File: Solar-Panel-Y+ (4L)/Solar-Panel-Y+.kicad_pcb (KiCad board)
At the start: 4 copper layers, 50 x 50 mm, 81 parts, among them J1 FTS-105-01-L-DV-A, Q1 BSS138DWQ-7, Q2 MBT2222ADW1T1, Q3 BSS138DWQ-7, Q4 MBT2222ADW1T1, U1 Value, U2 TSL2561

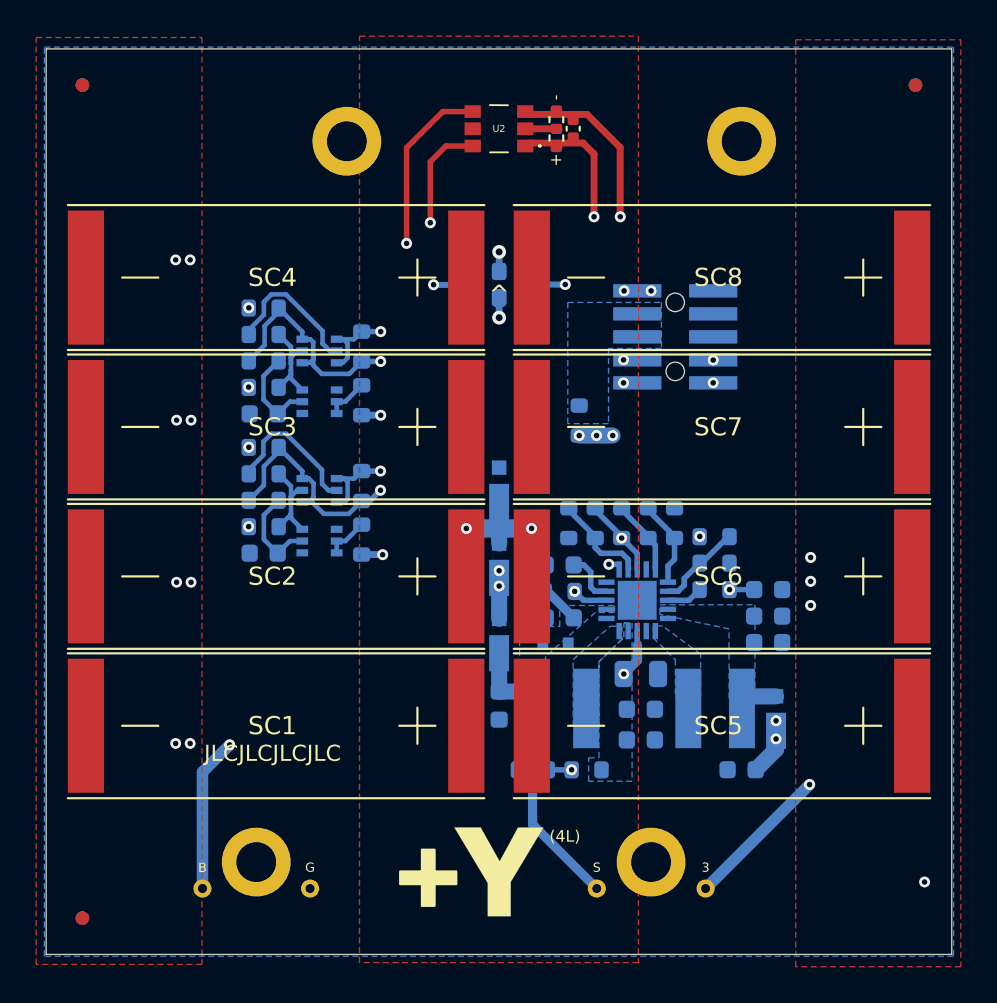
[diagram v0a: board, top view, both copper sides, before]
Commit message: Changed TSL2591 to BH1750
All boards (4L) except -Y
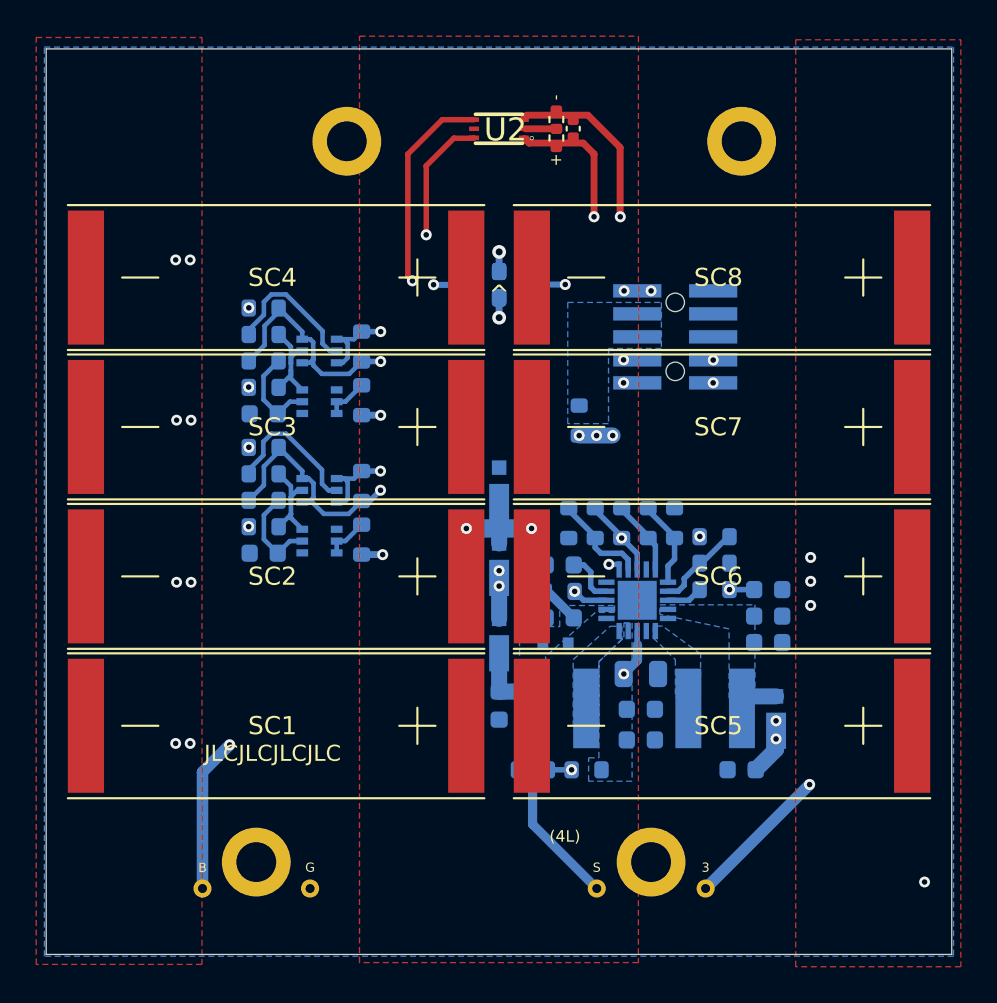
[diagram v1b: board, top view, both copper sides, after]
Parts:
- removed REF** (x6): Fiducial_0.75mm_Mask1.5mm, Fiducial:Fiducial_0.75mm_Mask1.5mm
- removed Ref**: Val**, custom-footprints:ypanel
- removed Ref**: Val**, custom-footprints:pycubed_mini_half
- U2: value TSL2561 -> BH1750FVI-TR; footprint solarpanels:TSL2561 -> solarpanels:WSOF6
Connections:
- U2 pad 4: SCL_LS -> SDA_LS
- U2 pad 6: SDA_LS -> SCL_LS
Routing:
- net SDA_LS: track 35.0 -> 36.8 mm
- net SCL_LS: track 29.7 -> 27.9 mm

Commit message: Updated light sensor to OPT 3001, Updated solar diodes.
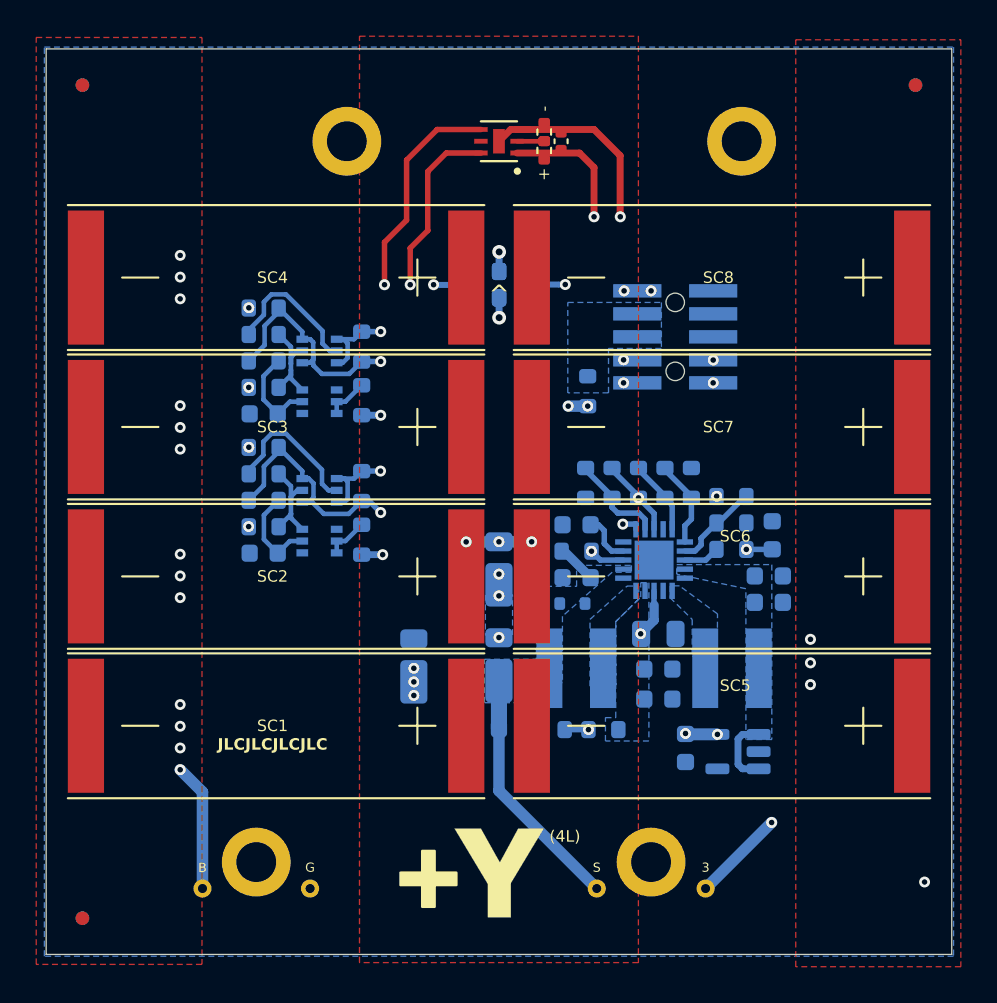
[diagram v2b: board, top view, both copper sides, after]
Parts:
- removed D5: MSS1P4-M3_89A, solarpanels:MICROSMP
- added ?: , , B.Cu at (81.6, 37.2)
- added REF**: Fiducial_0.75mm_Mask1.5mm, Fiducial:Fiducial_0.75mm_Mask1.5mm, F.Cu at (81.6, 83.2)
- added REF**: Fiducial_0.75mm_Mask1.5mm, Fiducial:Fiducial_0.75mm_Mask1.5mm, F.Cu at (81.6, 37.2)
- added REF**: Fiducial_0.75mm_Mask1.5mm, Fiducial:Fiducial_0.75mm_Mask1.5mm, F.Cu at (127.6, 37.2)
- added REF**: Fiducial_0.75mm_Mask1.5mm, Fiducial:Fiducial_0.75mm_Mask1.5mm, B.Cu at (81.6, 83.2)
- added REF**: Fiducial_0.75mm_Mask1.5mm, Fiducial:Fiducial_0.75mm_Mask1.5mm, B.Cu at (127.6, 37.2)
- added Ref**: Val**, custom-footprints:ypanel, F.Cu at (121.7, 81.6)
- added Ref**: Val**, custom-footprints:pycubed_mini_half, B.Cu at (104.7, 39.2)
- added U3: MAX40200AUK, Package_TO_SOT_SMD:SOT-23-5, B.Cu at (117.8, 74.0)
- D2, D3, D4: value MSS1P4-M3_89A -> DFLS130L-7; footprint solarpanels:MICROSMP -> Diode_SMD:D_PowerDI-123
- J1: value FTS-105-01-L-DV-A -> FTS-105-01-X-DV-A
- Q1, Q3: value BSS138DWQ-7 -> NX3008NBKS
- R1, R12, R13, R16, R17, R18, R2, R3, R4: value 0 -> 0R
- R14, R15: value DNI -> DNI (0R)
- R19: renamed from R21; value 680 -> DNI (0R)
- R20: renamed from R22; value 100K -> DNI (0R)
- R21: renamed from R19; value DNI -> 680R
- R22: renamed from R20; value DNI -> 100K
- R26: value 680 -> 680R
- U2: value BH1750FVI-TR -> OPT3001; footprint solarpanels:WSOF6 -> solarpanels:OPT3001
- moved D2 15.6 mm to (104.6, 69.2)
- moved D3 10.8 mm to (99.9, 69.3)
- moved R19 5.45 mm to (97.0, 51.6), turned to 90 degrees
- moved R21 5.45 mm to (91.6, 51.0), turned to 0 degrees
- moved R20 4.74 mm to (97.0, 59.3)
- moved R22 4.73 mm to (97.0, 54.6)
- moved C11 3.32 mm to (114.9, 73.8), turned to -90 degrees
- moved C6 3.01 mm to (119.7, 62.1), turned to 90 degrees
- moved C9 2.45 mm to (113.4, 71.1)
- moved C7 2.42 mm to (113.4, 69.4)
- moved C5 2.42 mm to (113.4, 67.5)
- moved R4 2.41 mm to (117.4, 62.8)
- moved C3 2.41 mm to (108.9, 64.4)
- moved C4 2.41 mm to (108.9, 61.5)
- moved D1 2.41 mm to (108.7, 65.8)
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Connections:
- C10 pad 1: Net-(C10-Pad1) -> Net-(U1-VOUT)
- C8 pad 1: Net-(C10-Pad1) -> Net-(U1-VOUT)
- D2 pad 1: +3V3 -> VSOLAR
- D2 pad 2: Net-(C10-Pad1) -> /VSOLAR_FULL
- L2 pad 2: Net-(C10-Pad1) -> Net-(U1-VOUT)
- Q1 pad 2: Net-(Q1-Pad2) -> Net-(Q1A-G2)
- Q1 pad 3: Net-(Q1-Pad2) -> Net-(Q1A-G2)
- Q1 pad 6: Net-(Q1-Pad6) -> Net-(Q1A-D1)
- Q2 pad 2: Net-(Q2-Pad2) -> Net-(Q2A-B1)
- Q2 pad 5: Net-(Q1-Pad6) -> Net-(Q1A-D1)
- R19 pad 1: Net-(Q2-Pad2) -> SCL_LS
- R19 pad 2: Net-(Q1-Pad6) -> SCL
- R20 pad 1: +3V3 -> SDA_LS
- R20 pad 2: Net-(Q1-Pad2) -> SDA
- R21 pad 1: SCL_LS -> Net-(Q2A-B1)
- R21 pad 2: SCL -> Net-(Q1A-D1)
- R22 pad 1: SDA_LS -> +3V3
- R22 pad 2: SDA -> Net-(Q1A-G2)
- R23 pad 2: Net-(Q1-Pad6) -> Net-(Q1A-D1)
- U1 pad 14: Net-(C10-Pad1) -> Net-(U1-VOUT)
- U2 pad 4: SDA_LS -> SCL_LS
- U2 pad 6: SCL_LS -> SDA_LS
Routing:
- net Net-(Q2A-B1): track 0.00 -> 7.79 mm
- net Net-(Q2-Pad2): track 7.79 -> 0.00 mm
- net Net-(Q1A-D1): track 0.00 -> 5.98 mm
- net Net-(Q1-Pad6): track 5.98 -> 0.00 mm
- net Net-(U1-VOUT): track 0.00 -> 3.88 mm
- net Net-(Q1A-G2): track 0.00 -> 2.40 mm
- net Net-(Q1-Pad2): track 2.40 -> 0.00 mm
- net VBAT: track 13.1 -> 10.8 mm, vias 5 -> 4
- net Net-(D3-K): track 5.89 -> 3.62 mm, vias 2 -> 6
- net Net-(C10-Pad1): track 2.05 -> 0.00 mm
- net SCL_LS: track 27.9 -> 29.9 mm
- net +3V3: track 20.2 -> 18.3 mm
- net VSOLAR: track 17.4 -> 15.8 mm
- net GND: track 10.0 -> 11.5 mm, vias 9 -> 13
- net VOUT_EN: track 9.16 -> 9.81 mm
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- added copper zone on B.Cu, net /VSOLAR_FULL
- added copper zone on B.Cu, net Net-(U1-VOUT)
- removed copper zone on B.Cu, net Net-(C10-Pad1)
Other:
- board text added: "Rev B3/01"
- board text removed: "Rev B2/01"

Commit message: Updated Mounting Holes
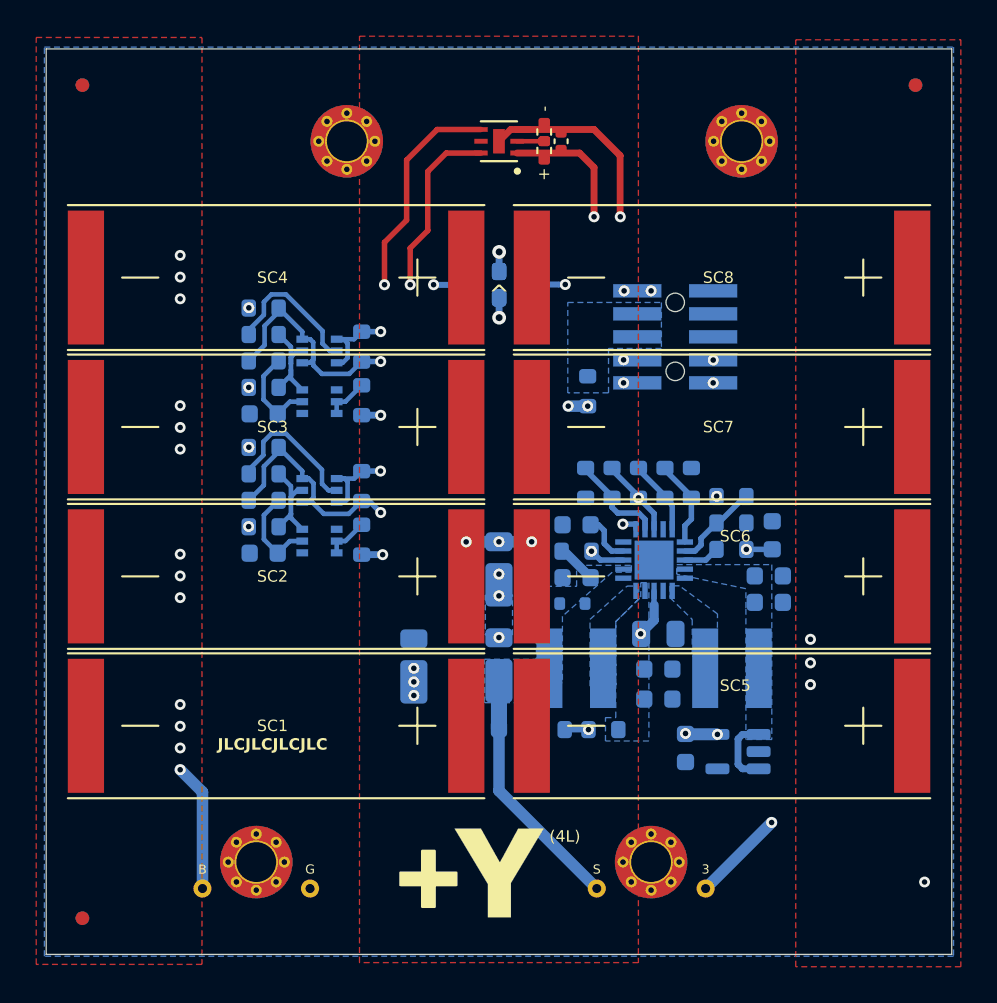
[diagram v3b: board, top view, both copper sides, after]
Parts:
- H1, H2, H3, H4: footprint MountingHole:MountingHole_2.2mm_M2_DIN965_Pad -> solarpanels:MountingHole_2.2mm_M2_DIN965_Pad_TopBottom

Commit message: B3/02 Updates
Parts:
- removed ?: , 
- added REF**: Fiducial_1mm_Mask2mm, Fiducial:Fiducial_1mm_Mask2mm, B.Cu at (81.6, 37.2)
- C1: value 1uF -> 0.1uF
- REF** (x5): value Fiducial_0.75mm_Mask1.5mm -> Fiducial_1mm_Mask2mm; footprint Fiducial:Fiducial_0.75mm_Mask1.5mm -> Fiducial:Fiducial_1mm_Mask2mm
- U1: value Value -> BQ25570RGRR
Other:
- board text added: "Rev B3/02"
- board text removed: "Rev B3/01"

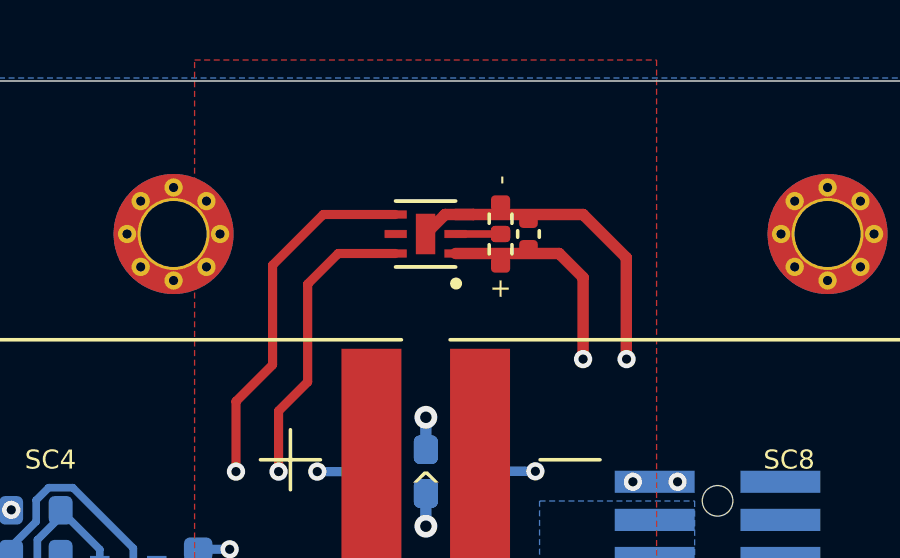
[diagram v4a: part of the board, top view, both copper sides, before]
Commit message: Updated Sun Sensor to OPT4001
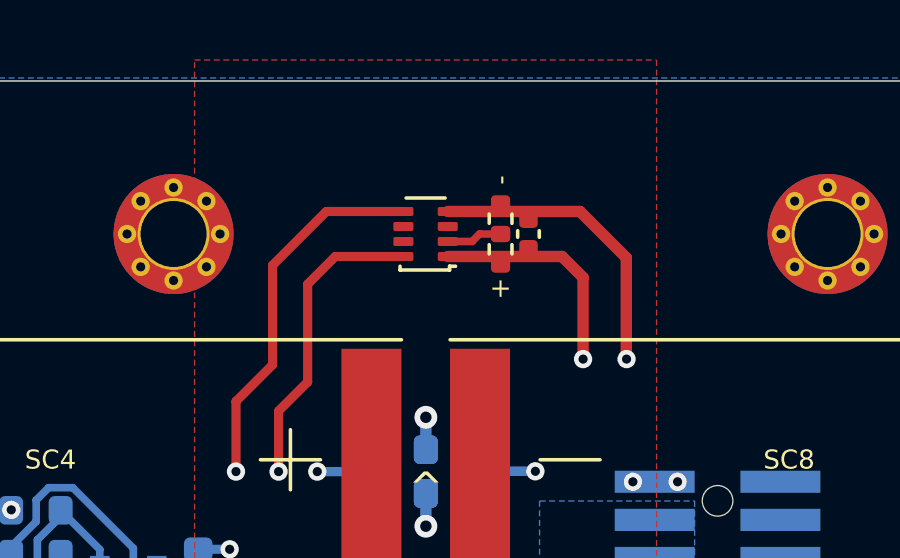
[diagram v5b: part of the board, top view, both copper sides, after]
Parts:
- U2: value OPT3001 -> OPT4001; footprint solarpanels:OPT3001 -> Package_TO_SOT_SMD:SOT-583-8
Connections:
- U2 pad 3: GND -> unconnected-(U2-NC-Pad3)
- U2 pad 4: SCL_LS -> GND
- U2 pad 5: unconnected-(U2-INT-Pad5) -> SCL_LS
- U2 pad 6: SDA_LS -> unconnected-(U2-NC-Pad6)
- U2 pad 7: GND -> unconnected-(U2-INT-Pad7)
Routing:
- net GND: track 11.5 -> 9.97 mm

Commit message: Updated Rev to B3/03
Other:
- board text added: "Rev B3/03"
- board text removed: "Rev B3/02"
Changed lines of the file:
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@@
     (effects (font (size 0.508 0.508) (thickness 0.1016)))
   )
-  (gr_text "Rev B3/02" (at 104.4 41.365) (layer "B.Mask")
+  (gr_text "Rev B3/03" (at 104.4 41.365) (layer "B.Mask")
     (effects (font (size 0.635 0.635) (thickness 0.1524)) (justify mirror))
   )
